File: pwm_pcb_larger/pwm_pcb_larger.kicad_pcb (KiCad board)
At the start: 2 copper layers, 88.2 x 74.4 mm, 75 parts, among them J1 Conn_01x02, J2 Conn_01x02, J3 Conn_01x16, Q1 NMOS, Q10 NMOS, Q11 NMOS, Q12 NMOS, Q13 NMOS, Q14 NMOS, Q15 NMOS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

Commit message: testing
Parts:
- turned G*** to -90 degrees
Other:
- board size 88.2 x 74.4 mm -> 88.2 x 70.4 mm
- board text added: "april 2023 rev.2"
- board text removed: "march 2023 rev.1"
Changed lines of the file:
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@@
   )
   (footprint "william_custom:freakylampsLogo_smaller" (layer "B.Cu")
-    (at 156.432327 68.9651 90)
+    (at 156.432327 68.9651 -90)
     (attr through_hole)
     (fp_text reference "G***" (at 0 0 90) (layer "B.SilkS") hide
@@
   (gr_circle (center 164.4 70) (end 165.8 68.8) (layer "B.SilkS") (width 0.15) (fill none))
   (gr_circle (center 164.6 69.6) (end 165.4 69.6) (layer "B.SilkS") (width 0.15) (fill none))
-  (gr_line (start 122.4 120.6) (end 98.6 122) (layer "Edge.Cuts") (width 0.1))
+  (gr_line (start 107.696 51.308) (end 97.536 51.562) (layer "B.Mask") (width 0.15))
+  (gr_line (start 97.282 56.134) (end 107.442 56.134) (layer "B.Mask") (width 0.15))
+  (gr_line (start 97.536 51.562) (end 97.282 56.134) (layer "B.Mask") (width 0.15))
+  (gr_line (start 107.442 56.134) (end 107.696 51.308) (layer "B.Mask") (width 0.15))
   (gr_line (start 172.6 81.8) (end 173.6 84) (layer "Edge.Cuts") (width 0.1))
   (gr_line (start 170.4 55.6) (end 168.6 59) (layer "Edge.Cuts") (width 0.1))
@@
   (gr_line (start 141.4 47.6) (end 161.2 48.4) (layer "Edge.Cuts") (width 0.1))
   (gr_line (start 168.6 59) (end 166.2 62.4) (layer "Edge.Cuts") (width 0.1))
-  (gr_line (start 165.2 118) (end 153 121) (layer "Edge.Cuts") (width 0.1))
+  (gr_line (start 94.742 117.602) (end 165.2 118) (layer "Edge.Cuts") (width 0.1))
   (gr_line (start 114 47.8) (end 141.4 47.6) (layer "Edge.Cuts") (width 0.1))
   (gr_line (start 169.4 90) (end 166.8 94.8) (layer "Edge.Cuts") (width 0.1))
@@
   (gr_line (start 166.8 94.8) (end 167.8 97.8) (layer "Edge.Cuts") (width 0.1))
   (gr_arc (start 88.2 114.2) (mid 86.692802 110.544407) (end 87.571629 106.689194) (layer "Edge.Cuts") (width 0.1))
-  (gr_line (start 153 121) (end 122.4 120.6) (layer "Edge.Cuts") (width 0.1))
   (gr_line (start 161.2 48.4) (end 168.6 51.4) (layer "Edge.Cuts") (width 0.1))
+  (gr_line (start 88.8 116.4) (end 94.742 117.602) (layer "Edge.Cuts") (width 0.1))
   (gr_line (start 168.6 51.4) (end 170.4 55.6) (layer "Edge.Cuts") (width 0.1))
   (gr_line (start 168.2 69.8) (end 167 76.8) (layer "Edge.Cuts") (width 0.1))
@@
   (gr_line (start 88.8 116.4) (end 88.2 114.2) (layer "Edge.Cuts") (width 0.1))
   (gr_line (start 170.2 103) (end 171.4 104.8) (layer "Edge.Cuts") (width 0.1))
-  (gr_line (start 98.6 122) (end 88.8 116.4) (layer "Edge.Cuts") (width 0.1))
   (gr_arc (start 87.4 51.8) (mid 90.80844 49.401468) (end 94.943202 49.925077) (layer "Edge.Cuts") (width 0.1))
+  (gr_text "april 2023\nrev.2" (at 162.56 80.518 90) (layer "B.Cu")
+    (effects (font (size 1 1) (thickness 0.25) italic) (justify mirror))
+  )
   (gr_text "5v OR 8-37V !" (at 95.6 82.4 270) (layer "B.SilkS")
     (effects (font (size 1.5 1.5) (thickness 0.15)) (justify mirror))
@@
     (effects (font (size 2 2) (thickness 0.15)) (justify mirror))
   )
+  (gr_text "april 2023\nrev.2" (at 162.052 80.518 90) (layer "B.SilkS")
+    (effects (font (size 1 1) (thickness 0.25) italic) (justify mirror))
+  )
   (gr_text "10 11 12 13 14 15 16" (at 109.4 108.8) (layer "B.SilkS")
     (effects (font (size 1 1.45) (thickness 0.15)) (justify mirror))
@@
     (effects (font (size 2 2) (thickness 0.5) italic) (justify mirror))
   )
-  (gr_text "march 2023\nrev.1" (at 152.6 78.6 90) (layer "B.Mask")
+  (gr_text "april 2023\nrev.2" (at 162.56 80.518 90) (layer "B.Mask")
     (effects (font (size 1 1) (thickness 0.25) italic) (justify mirror))
   )
@@
       )
     )
+  )
+  (zone (net 0) (net_name "") (layer "B.Mask") (hatch edge 0.508)
+    (connect_pads (clearance 0.508))
+    (min_thickness 0.254) (filled_areas_thickness no)
+    (fill yes (thermal_gap 0.508) (thermal_bridge_width 0.508))
+    (polygon
+      (pts
+        (xy 107.442 56.134)
+        (xy 97.282 56.134)
+        (xy 97.028 51.562)
+        (xy 97.536 51.562)
+        (xy 107.696 51.308)
+      )
+    )

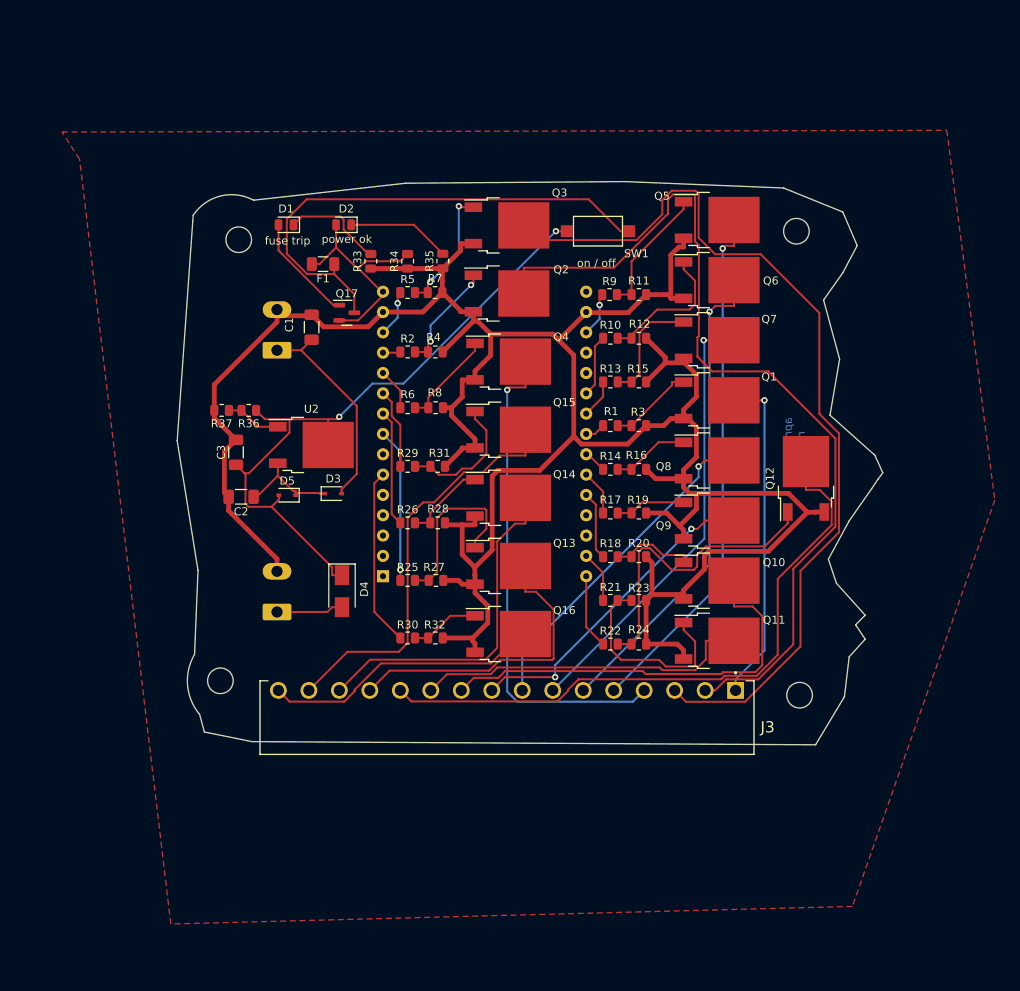
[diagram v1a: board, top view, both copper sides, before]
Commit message: updating the new rev board with new connectors for led outputs and PSU input
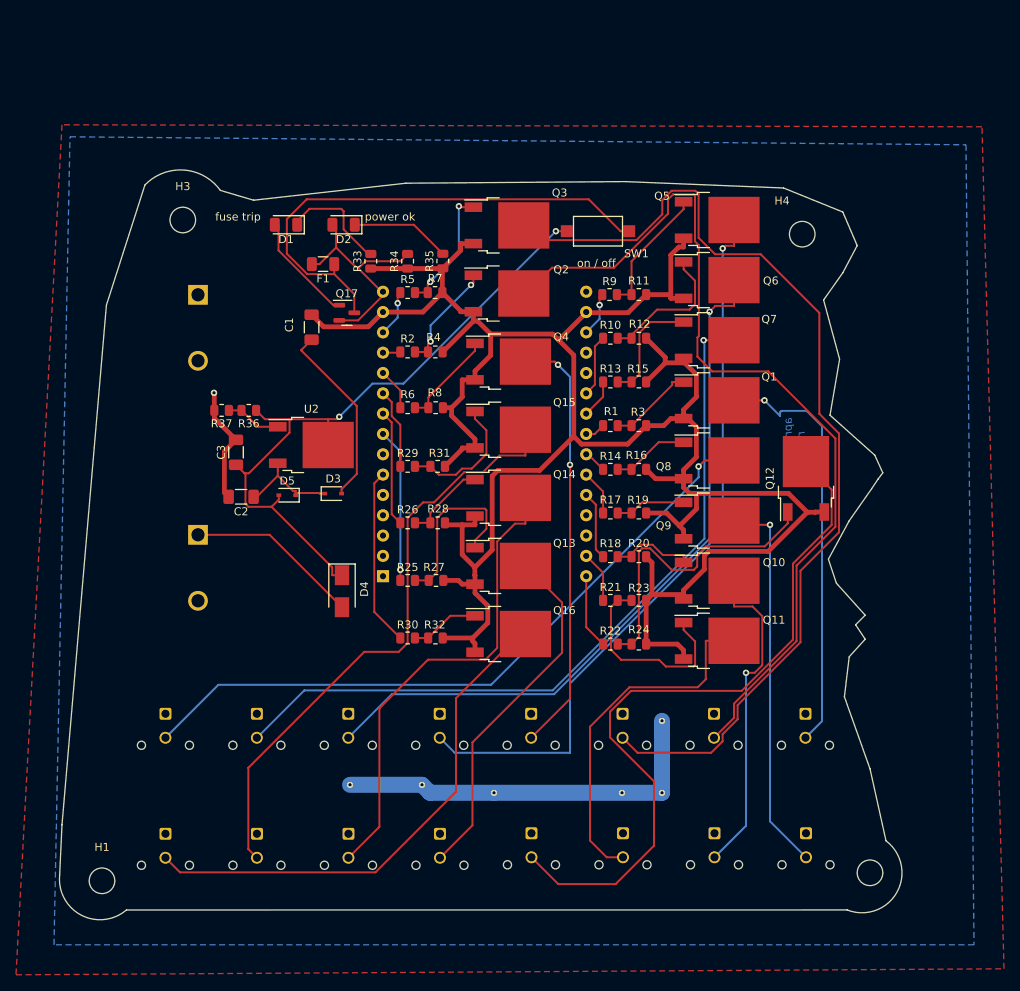
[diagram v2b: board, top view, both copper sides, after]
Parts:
- removed G***: LOGO, william_custom:freakylampsLogo_smaller
- removed MH1, MH2, MH3, MH4: MountingHole_3.2mm_M3, MountingHole:MountingHole_3.2mm_M3
- added H1: MountingHole, MountingHole:MountingHole_3.2mm_M3, F.Cu at (76.0, 135.0)
- added H2: MountingHole, MountingHole:MountingHole_3.2mm_M3, F.Cu at (172.0, 134.0)
- added H3: MountingHole, MountingHole:MountingHole_3.2mm_M3, F.Cu at (86.1, 52.4)
- added H4: MountingHole, MountingHole:MountingHole_3.2mm_M3, F.Cu at (163.5, 54.2)
- added J10: Conn_01x02, Connector_Molex:Molex_Micro-Fit_3.0_43045-0212_2x01_P3.00mm_Vertical, B.Cu at (83.9, 114.1)
- added J11: Conn_01x02, Connector_Molex:Molex_Micro-Fit_3.0_43045-0212_2x01_P3.00mm_Vertical, B.Cu at (164.0, 129.1)
- added J12: Conn_01x02, Connector_Molex:Molex_Micro-Fit_3.0_43045-0212_2x01_P3.00mm_Vertical, B.Cu at (152.6, 129.1)
- added J13: Conn_01x02, Connector_Molex:Molex_Micro-Fit_3.0_43045-0212_2x01_P3.00mm_Vertical, B.Cu at (141.1, 129.1)
- added J14: Conn_01x02, Connector_Molex:Molex_Micro-Fit_3.0_43045-0212_2x01_P3.00mm_Vertical, B.Cu at (129.7, 129.1)
- added J15: Conn_01x02, Connector_Molex:Molex_Micro-Fit_3.0_43045-0212_2x01_P3.00mm_Vertical, B.Cu at (118.2, 129.1)
- added J16: Conn_01x02, Connector_Molex:Molex_Micro-Fit_3.0_43045-0212_2x01_P3.00mm_Vertical, B.Cu at (106.8, 129.1)
- added J17: Conn_01x02, Connector_Molex:Molex_Micro-Fit_3.0_43045-0212_2x01_P3.00mm_Vertical, B.Cu at (95.4, 129.1)
- added J18: Conn_01x02, Connector_Molex:Molex_Micro-Fit_3.0_43045-0212_2x01_P3.00mm_Vertical, B.Cu at (83.9, 129.1)
- added J4: Conn_01x02, Connector_Molex:Molex_Micro-Fit_3.0_43045-0212_2x01_P3.00mm_Vertical, B.Cu at (152.5, 114.1)
- added J5: Conn_01x02, Connector_Molex:Molex_Micro-Fit_3.0_43045-0212_2x01_P3.00mm_Vertical, B.Cu at (141.1, 114.1)
- added J6: Conn_01x02, Connector_Molex:Molex_Micro-Fit_3.0_43045-0212_2x01_P3.00mm_Vertical, B.Cu at (129.6, 114.1)
- added J7: Conn_01x02, Connector_Molex:Molex_Micro-Fit_3.0_43045-0212_2x01_P3.00mm_Vertical, B.Cu at (118.2, 114.1)
- added J8: Conn_01x02, Connector_Molex:Molex_Micro-Fit_3.0_43045-0212_2x01_P3.00mm_Vertical, B.Cu at (106.8, 114.1)
- added J9: Conn_01x02, Connector_Molex:Molex_Micro-Fit_3.0_43045-0212_2x01_P3.00mm_Vertical, B.Cu at (95.4, 114.1)
- D1, D2: footprint LED_SMD:LED_0805_2012Metric -> LED_SMD:LED_1206_3216Metric
- J1, J2: footprint Connector_Phoenix_MSTB:PhoenixContact_MSTBVA_2,5_2-G-5,08_1x02_P5.08mm_Vertical -> william customs:Kobiconn - 2 pin terminal - 158P02DT39BE
- J3: value Conn_01x16 -> Conn_01x02; footprint william_custom:CUI_TBP02R1-381-16BE -> Connector_Molex:Molex_Micro-Fit_3.0_43045-0212_2x01_P3.00mm_Vertical; moved to B.Cu
- moved J2 13.8 mm to (88.0, 91.8), turned to -90 degrees
- moved J1 12.1 mm to (88.0, 61.8), turned to -90 degrees
- moved J3 9.21 mm to (163.9, 114.1)
- moved G1 5.23 mm to (149.5, 98.5)
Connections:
- J3 pad 1: LED_1 -> +VDC
- J3 pad 2: LED_2 -> LED_1
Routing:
- net +VDC: track 26.5 -> 71.9 mm, vias 0 -> 6
- net LED_8: track 41.9 -> 86.2 mm
- net LED_7: track 55.5 -> 94.9 mm
- net LED_6: track 60.5 -> 90.4 mm
- net LED_16: track 35.1 -> 64.9 mm
- net GND: track 347.1 -> 317.4 mm, vias 0 -> 1
- net LED_5: track 65.7 -> 92.8 mm
- net LED_15: track 51.6 -> 74.9 mm
- net LED_14: track 42.9 -> 59.1 mm
- net Net-(D4-A): track 8.37 -> 21.7 mm
- net LED_10: track 52.6 -> 40.5 mm, vias 0 -> 1
- net LED_1: track 41.6 -> 52.9 mm
- net LED_3: track 114.7 -> 125.3 mm
- net LED_12: track 79.5 -> 89.9 mm
- net LED_9: track 40.0 -> 48.1 mm, vias 2 -> 1
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- added copper zone on F.Cu, net +VDC
- added copper zone on B.Cu, net GND
- removed copper zone on F.Cu, net GND
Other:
- board size 88.2 x 70.4 mm -> 105.3 x 93.7 mm
- board text added: "5v OR 8-37V !!!!"
- board text added: "LED outputs!"
- board text added: "LED1"
- board text added: "LED10"
- board text added: "LED11"
- board text added: "LED12"
- board text added: "LED13"
- board text added: "LED14"
- board text added: "LED15"
- board text added: "LED16"
- board text added: "LED2"
- board text added: "LED3"
- board text added: "LED4"
- board text added: "LED5"
- board text added: "LED6"
- board text added: "LED7"
- board text added: "LED8"
- board text added: "LED9"
- board text added: "May 2024 rev.3"
- board text added: "S/N#:"
- board text removed: "1 2 3 4 5 6 7 8 9"
- board text removed: "10 11 12 13 14 15 16"
- board text removed: "5v OR 8-37V !"
- board text removed: "LED inputs! Plug Negative side of leds here. Common Positive"

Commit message: rev 3 finished and sent to JLC for fab
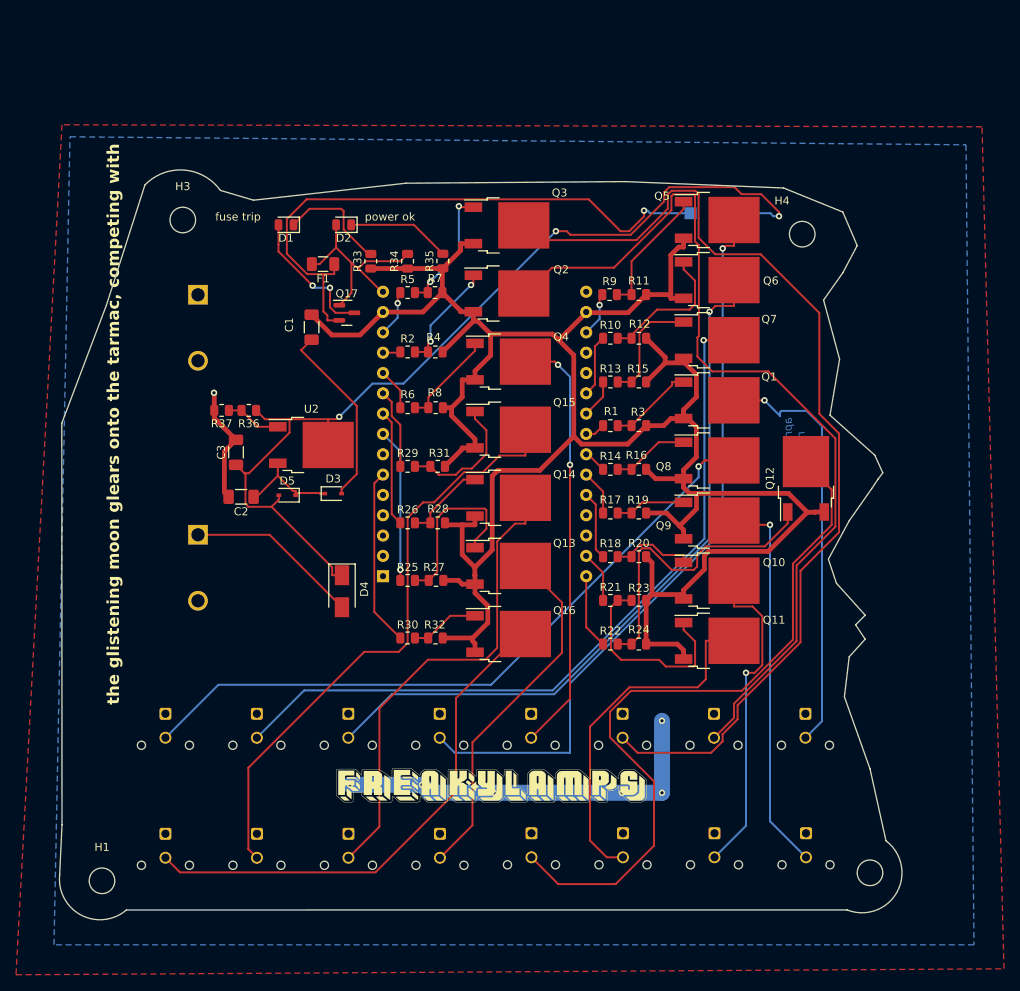
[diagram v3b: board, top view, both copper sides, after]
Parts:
- added G***: LOGO, william_custom:freakylampsLogo_smaller, F.Cu at (124.5, 123.4)
- added G***: LOGO, william_custom:freakylampsLogo_smaller, B.Cu at (74.1, 112.6)
- D1, D2: footprint LED_SMD:LED_1206_3216Metric -> LED_SMD:LED_0805_2012Metric
- SW1: moved to B.Cu
- moved SW1 15.6 mm to (153.5, 51.5), turned to 180 degrees
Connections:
- F1 pad 1: Net-(Q17-S) -> Net-(Q17-D)
- Q17 pad 1: Net-(D1-A) -> esp32_power
- Q17 pad 2: esp32_power -> Net-(Q17-D)
- Q17 pad 3: Net-(Q17-S) -> Net-(D1-A)
- SW1 pad 2: Net-(Q17-S) -> Net-(Q17-D)
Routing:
- net Net-(Q17-D): track 0.00 -> 74.8 mm, vias 0 -> 1
- net Net-(Q17-S): track 63.9 -> 0.00 mm
- net +5V: track 85.1 -> 120.2 mm, vias 2 -> 3
- net Net-(D1-A): track 13.6 -> 17.4 mm, vias 0 -> 2
- net GND: track 317.4 -> 318.3 mm
- net esp32_power: track 29.0 -> 28.2 mm
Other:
- outline, holes or cut-outs redrawn
- board text added: "power fuse trip"
- board text added: "the glistening moon glears onto the tarmac, competing with"
- board text added: "the sunset through the stucco walls"
